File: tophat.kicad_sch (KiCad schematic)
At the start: 22 parts, among them J1 Power, J2 Digital/PWM, J3 Analog, J4 Digital/PWM, J5 Conn_01x03_Socket, J6 Conn_01x03_Socket, J7 Conn_01x03_Socket, U1 74LVC2G241, U2 TXB0104PW

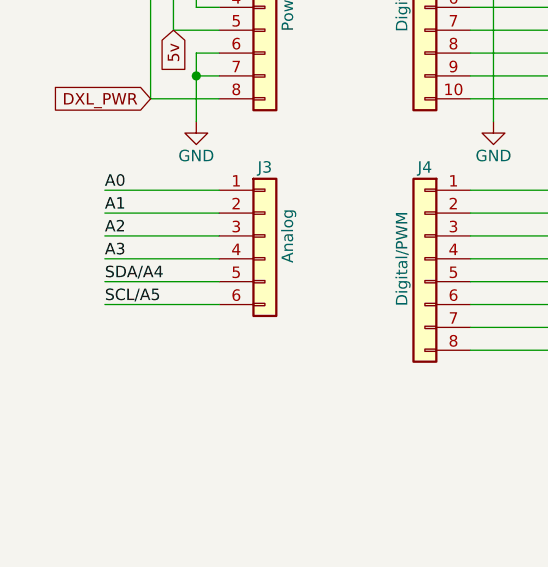
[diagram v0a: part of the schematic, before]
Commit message: Add silk screen and fix up schematic
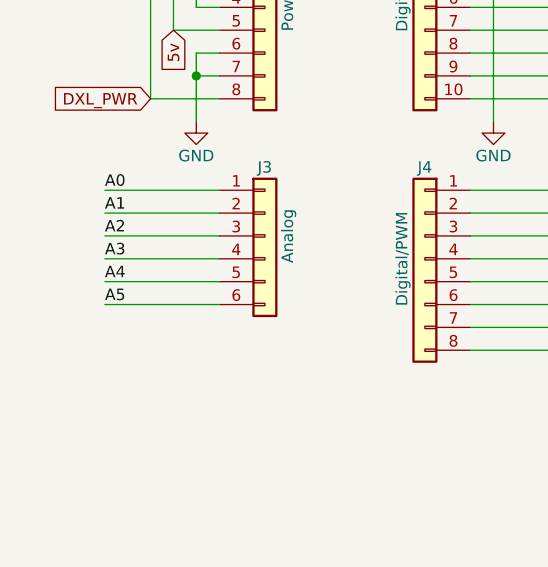
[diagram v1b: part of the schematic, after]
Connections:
- net SCL/A5: no longer J3.6 (Pin_6)
- net SDA/A4: no longer J3.5 (Pin_5)
- new net A4: J3.5 (Pin_5)
- new net A5: J3.6 (Pin_6)
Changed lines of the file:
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@@
+		)
+	)
+	(label "A5"
+		(at 21.59 72.39 0)
+		(fields_autoplaced yes)
+		(effects
+			(font
+				(size 1.27 1.27)
+			)
+			(justify left bottom)
 		)
 	)
@@
 		)
 	)
+	(label "A4"
+		(at 21.59 69.85 0)
+		(fields_autoplaced yes)
+		(effects
+			(font
+				(size 1.27 1.27)
+			)
+			(justify left bottom)
+		)
+	)
 	(label "Vin"
 		(at 26.67 26.67 270)
@@
 		(fields_autoplaced yes)
 		(effects
-			(font
-				(size 1.27 1.27)
-			)
-			(justify left bottom)
-		)
-	)
-	(label "SDA{slash}A4"
-		(at 21.59 69.85 0)
-		(fields_autoplaced yes)
-		(effects
-			(font
-				(size 1.27 1.27)
-			)
-			(justify left bottom)
-		)
-	)
-	(label "SCL{slash}A5"
-		(at 21.59 72.39 0)
-		(fields_autoplaced yes)
-		(effects
